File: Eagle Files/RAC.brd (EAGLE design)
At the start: 100 x 78.7 mm, 9 parts

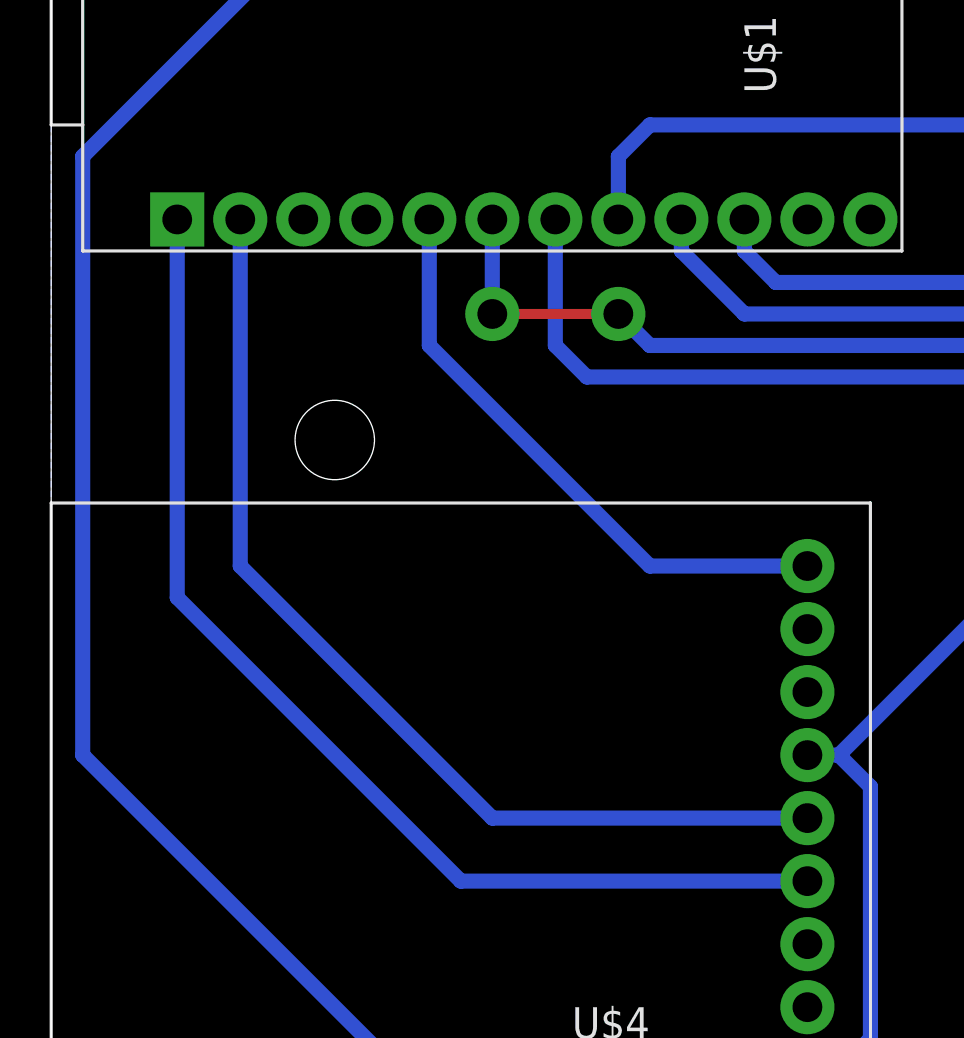
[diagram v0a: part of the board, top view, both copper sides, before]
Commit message: Corrige inversión de pines TX y RX para BLE
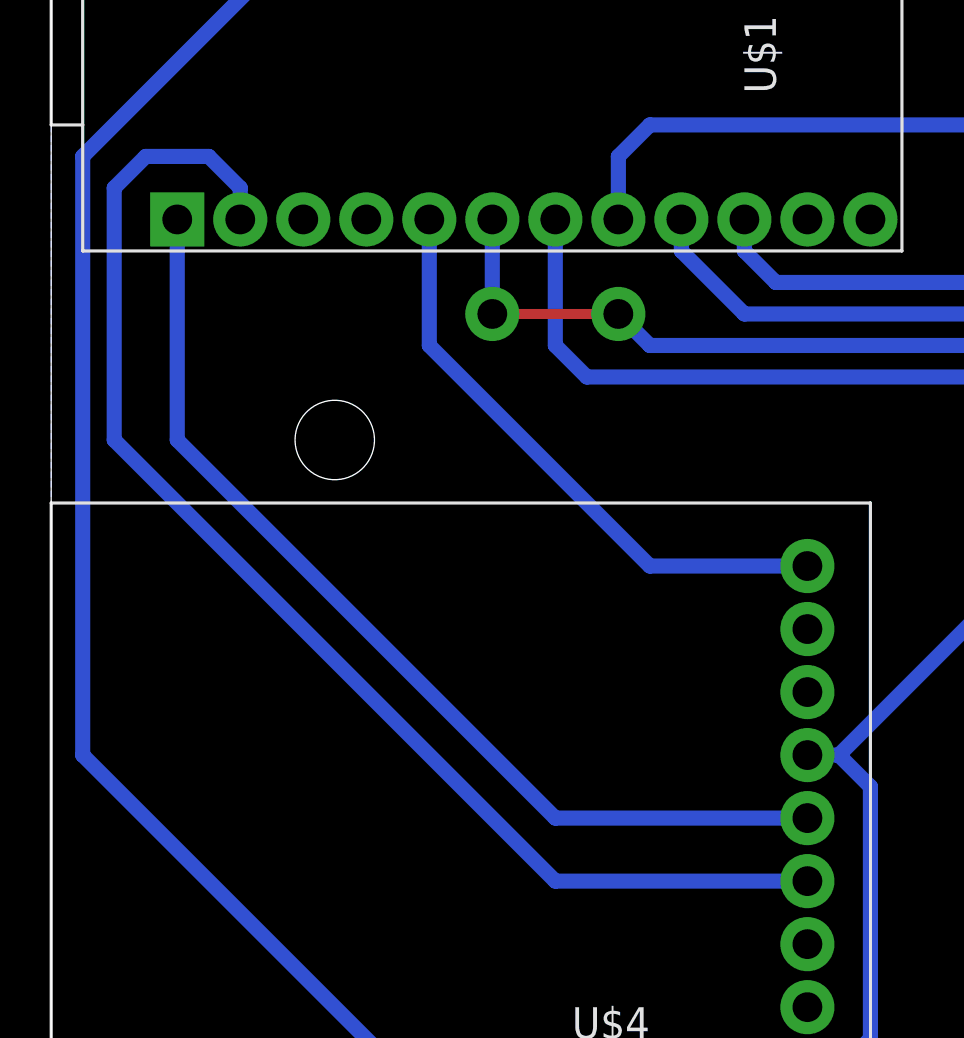
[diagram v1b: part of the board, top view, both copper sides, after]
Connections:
- removed net N$17: U$1.0, U$4.RX
- new net S$4: U$1.1, U$4.RX
- net N$18: now also U$1.0; no longer U$1.1
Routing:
- net N$17: track 41.0 -> 0.00 mm
- net S$4: track 0.00 -> 40.6 mm
- net N$18: track 45.4 -> 52.9 mm
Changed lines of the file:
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@@
 <wire x1="19.05" y1="59.69" x2="21.59" y2="59.69" width="0.6096" layer="16"/>
 </signal>
-<signal name="N$17">
+<signal name="S$4">
 <contactref element="U$4" pad="RX"/>
-<contactref element="U$1" pad="0"/>
-<wire x1="7.62" y1="36.83" x2="7.62" y2="22.86" width="0.6096" layer="16"/>
-<wire x1="7.62" y1="22.86" x2="17.78" y2="12.7" width="0.6096" layer="16"/>
-<wire x1="17.78" y1="12.7" x2="30.48" y2="12.7" width="0.6096" layer="16"/>
+<contactref element="U$1" pad="1"/>
+<wire x1="30.48" y1="12.7" x2="20.32" y2="12.7" width="0.6096" layer="16"/>
+<wire x1="20.32" y1="12.7" x2="5.08" y2="27.94" width="0.6096" layer="16"/>
+<wire x1="5.08" y1="27.94" x2="5.08" y2="36.83" width="0.6096" layer="16"/>
 </signal>
 <signal name="N$18">
 <contactref element="U$4" pad="TX"/>
-<contactref element="U$1" pad="1"/>
-<wire x1="30.48" y1="10.16" x2="16.51" y2="10.16" width="0.6096" layer="16"/>
-<wire x1="16.51" y1="10.16" x2="5.08" y2="21.59" width="0.6096" layer="16"/>
-<wire x1="5.08" y1="21.59" x2="5.08" y2="36.83" width="0.6096" layer="16"/>
+<contactref element="U$1" pad="0"/>
+<wire x1="30.48" y1="10.16" x2="20.32" y2="10.16" width="0.6096" layer="16"/>
+<wire x1="20.32" y1="10.16" x2="2.54" y2="27.94" width="0.6096" layer="16"/>
+<wire x1="2.54" y1="27.94" x2="2.54" y2="38.1" width="0.6096" layer="16"/>
+<wire x1="2.54" y1="38.1" x2="3.81" y2="39.37" width="0.6096" layer="16"/>
+<wire x1="3.81" y1="39.37" x2="6.35" y2="39.37" width="0.6096" layer="16"/>
+<wire x1="6.35" y1="39.37" x2="7.62" y2="38.1" width="0.6096" layer="16"/>
+<wire x1="7.62" y1="38.1" x2="7.62" y2="36.83" width="0.6096" layer="16"/>
 </signal>
 <signal name="N$19">
